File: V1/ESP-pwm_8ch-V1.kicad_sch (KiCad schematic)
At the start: 45 parts, among them J1 12VDC, J2 CH1/2, J3 CH3/4, J4 CH5/6, J5 CH7/8, Q1 IRLB8721PBF, Q2 IRLB8721PBF, Q3 IRLB8721PBF, Q4 IRLB8721PBF, Q5 IRLB8721PBF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

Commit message: work in progress
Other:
- title: ESP 6x PWM Module -> ESP 8x PWM Module
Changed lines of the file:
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@@
   (paper "A3")
   (title_block
-    (title "ESP 6x PWM Module")
+    (title "ESP 8x PWM Module")
     (date "2022-03-26")
     (rev "2")

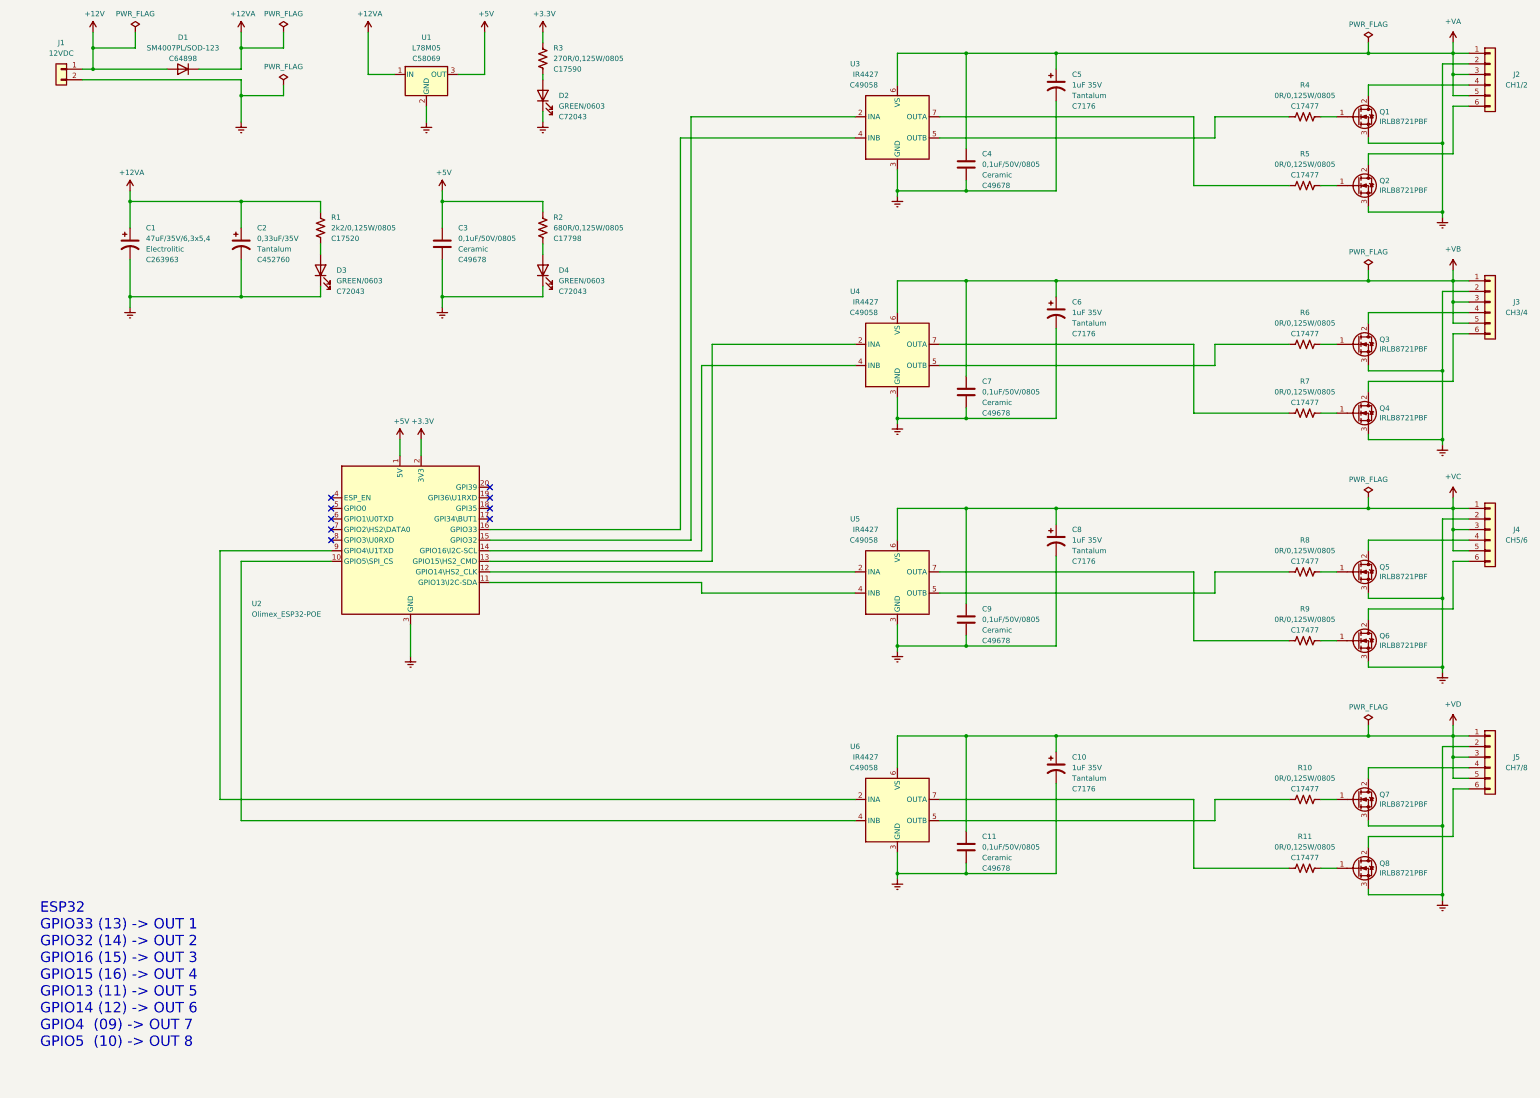
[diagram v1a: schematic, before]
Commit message: Updated MOSFET gate resistor
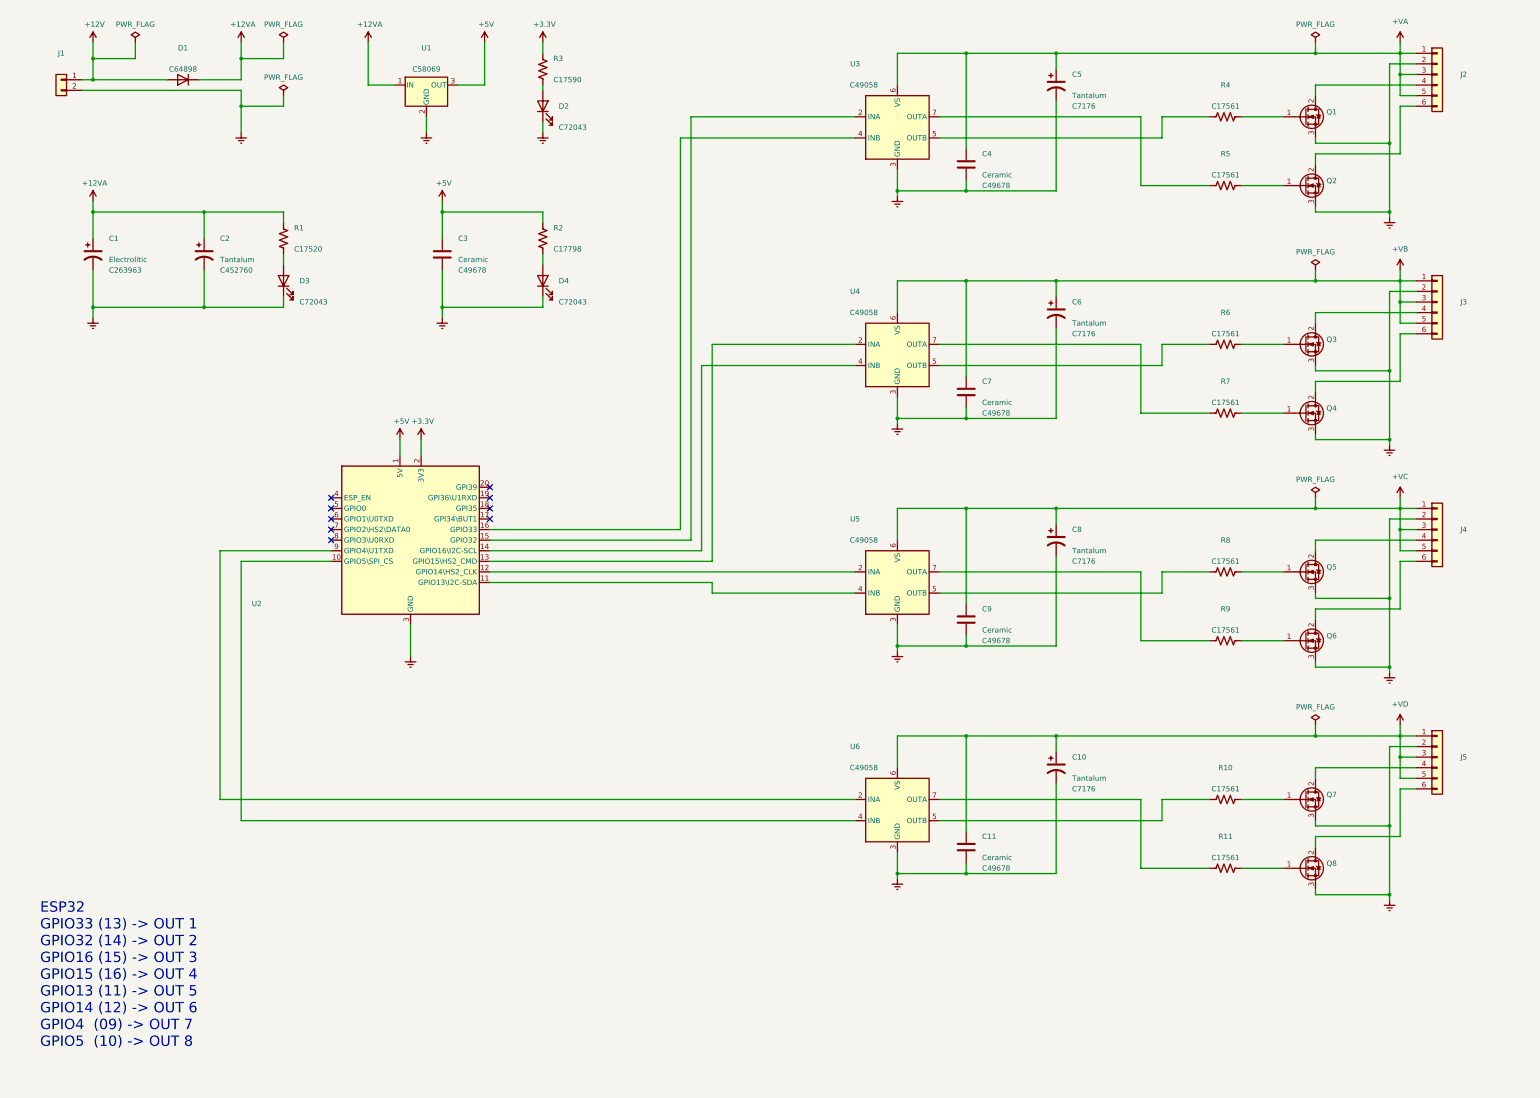
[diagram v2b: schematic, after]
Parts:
- C1: value 47uF/35V/6,3x5,4 -> (none); footprint Tales:CP_Elec_6.3x5.4 -> (none)
- C10, C5, C6, C8: value 1uF 35V -> (none); footprint Tales:CP_EIA-3216-18_Kemet-A_Pad1.58x1.35mm_HandSolder -> (none)
- C11, C3, C4, C7, C9: value 0,1uF/50V/0805 -> (none); footprint Tales:C_0805_2012Metric -> (none)
- C2: value 0,33uF/35V -> (none); footprint Tales:CP_EIA-3216-18_Kemet-A_Pad1.58x1.35mm_HandSolder -> (none)
- D1: value SM4007PL/SOD-123 -> (none); footprint Tales:D_SOD-123 -> (none)
- D2, D3, D4: value GREEN/0603 -> (none); footprint Tales:LED_0603_1608Metric -> (none)
- J1: value 12VDC -> (none); footprint Tales:TerminalBlock_Phoenix_MKDS-3-2-5.08_1x02_P5.08mm_Horizontal -> (none)
- J2: value CH1/2 -> (none); footprint Tales:TerminalBlock_Phoenix_MKDS-3-6-5.08_1x06_P5.08mm_Horizontal -> (none)
- J3: value CH3/4 -> (none); footprint Tales:TerminalBlock_Phoenix_MKDS-3-6-5.08_1x06_P5.08mm_Horizontal -> (none)
- J4: value CH5/6 -> (none); footprint Tales:TerminalBlock_Phoenix_MKDS-3-6-5.08_1x06_P5.08mm_Horizontal -> (none)
- J5: value CH7/8 -> (none); footprint Tales:TerminalBlock_Phoenix_MKDS-3-6-5.08_1x06_P5.08mm_Horizontal -> (none)
- Q1, Q2, Q3, Q4, Q5, Q6, Q7, Q8: value IRLB8721PBF -> (none); footprint Tales:TO-220-3_Vertical -> (none)
- R1: value 2k2/0,125W/0805 -> (none); footprint Tales:R_0805_2012Metric -> (none)
- R10, R11, R4, R5, R6, R7, R8, R9: value 0R/0,125W/0805 -> (none); footprint Tales:R_0805_2012Metric -> (none); LCSC Part C17477 -> C17561; Mfr PN 0805W8F0000T5E -> 0805W8F220JT5E; Vendor PN C17477 -> C17561
- R2: value 680R/0,125W/0805 -> (none); footprint Tales:R_0805_2012Metric -> (none)
- R3: value 270R/0,125W/0805 -> (none); footprint Tales:R_0805_2012Metric -> (none)
- U1: value L78M05 -> (none); footprint Tales:TO-252-2 -> (none)
- U2: value Olimex_ESP32-POE -> (none); footprint Tales:Olimex_ESP32-POE_Pads -> (none)
- U3, U4, U5, U6: value IR4427 -> (none); footprint Tales:SOIC-8_3.9x4.9mm_P1.27mm -> (none)
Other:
- moved on the sheet: C1, C2, C3, D1, D2, D3, D4, J1, J2, J3, J4, J5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

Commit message: Added ESP8266
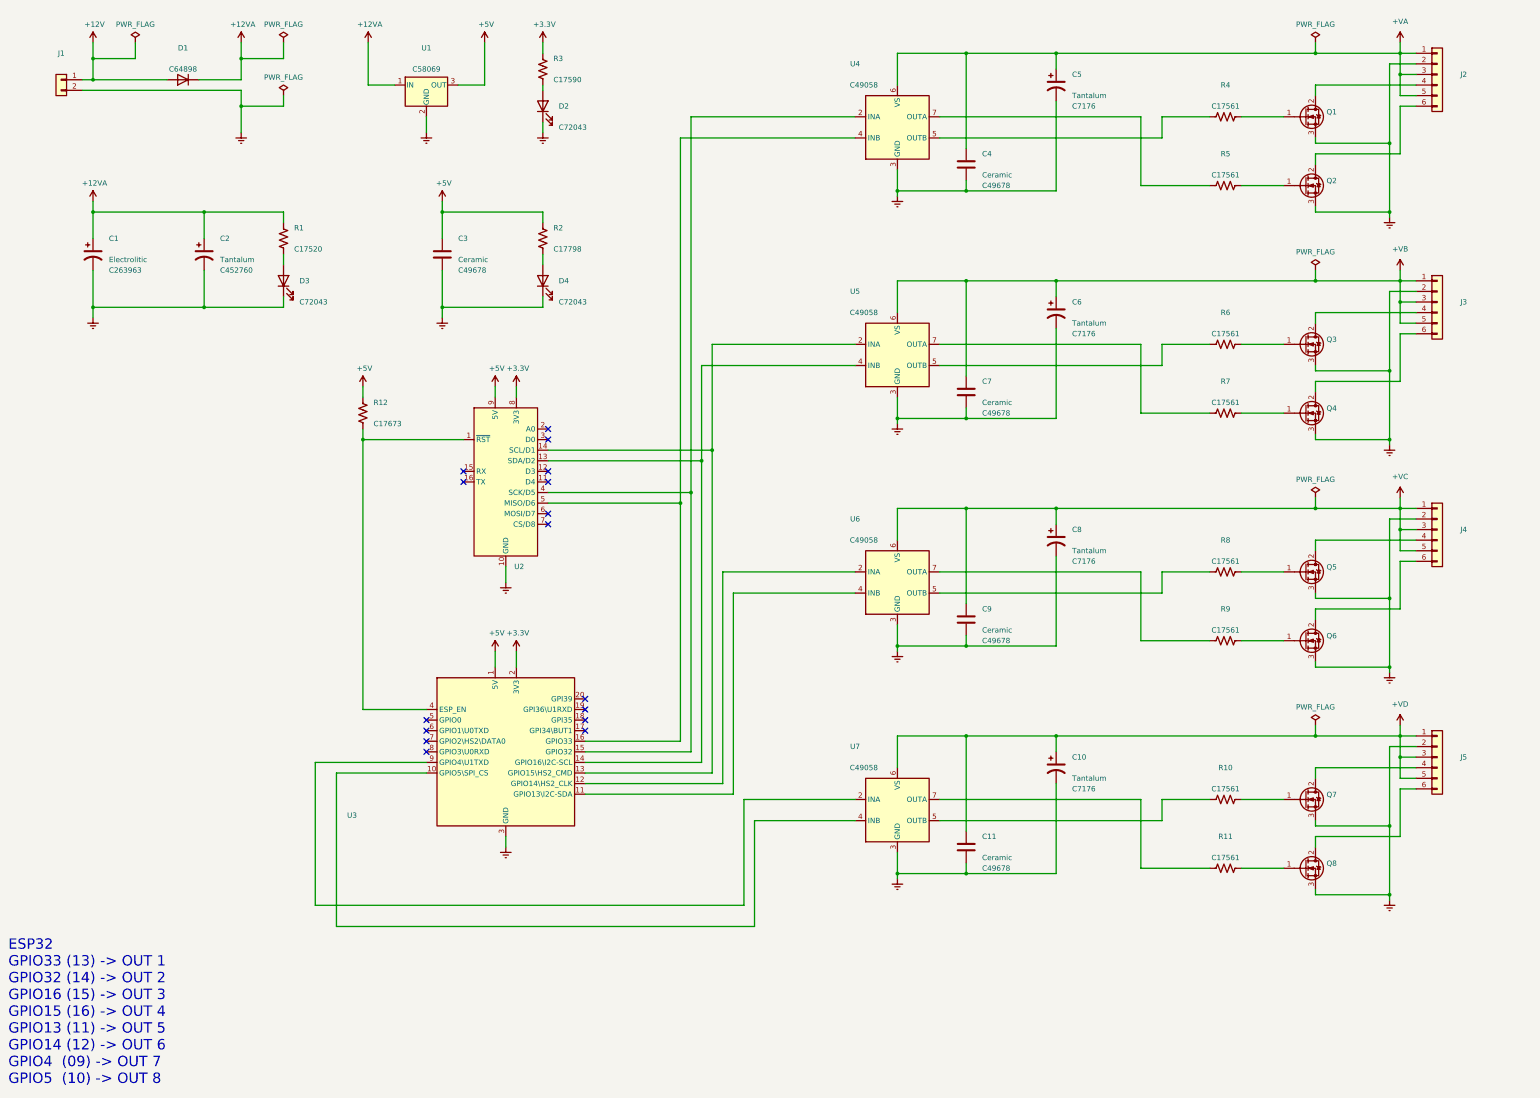
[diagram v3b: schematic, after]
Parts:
- added R12: (no value), symbol Device:R_US
- added U2: (no value), symbol MCU_Module:WeMos_D1_mini
- renumbered U2 to U3, U3 to U4, U4 to U5, U5 to U6, U6 to U7
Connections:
- net +3V3: now also U2.8 (3V3)
- net +5V: now also R12.1, U2.9 (5V)
- net GNDREF: now also U2.10 (GND)
- net at U3.13 (GPIO15\HS2_CMD), U5.2 (INA): now also U2.14 (SCL/D1)
- net at U3.14 (GPIO16\I2C-SCL), U5.4 (INB): now also U2.13 (SDA/D2)
- net at U3.15 (GPIO32), U4.2 (INA): now also U2.4 (SCK/D5)
- net at U3.16 (GPIO33), U4.4 (INB): now also U2.5 (MISO/D6)
- net at U3.4 (ESP_EN): now also R12.2, U2.1 (~{RST})
- no-connect marks 9 -> 16
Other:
- moved on the sheet: U3

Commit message: Reset pull up to +3.3V
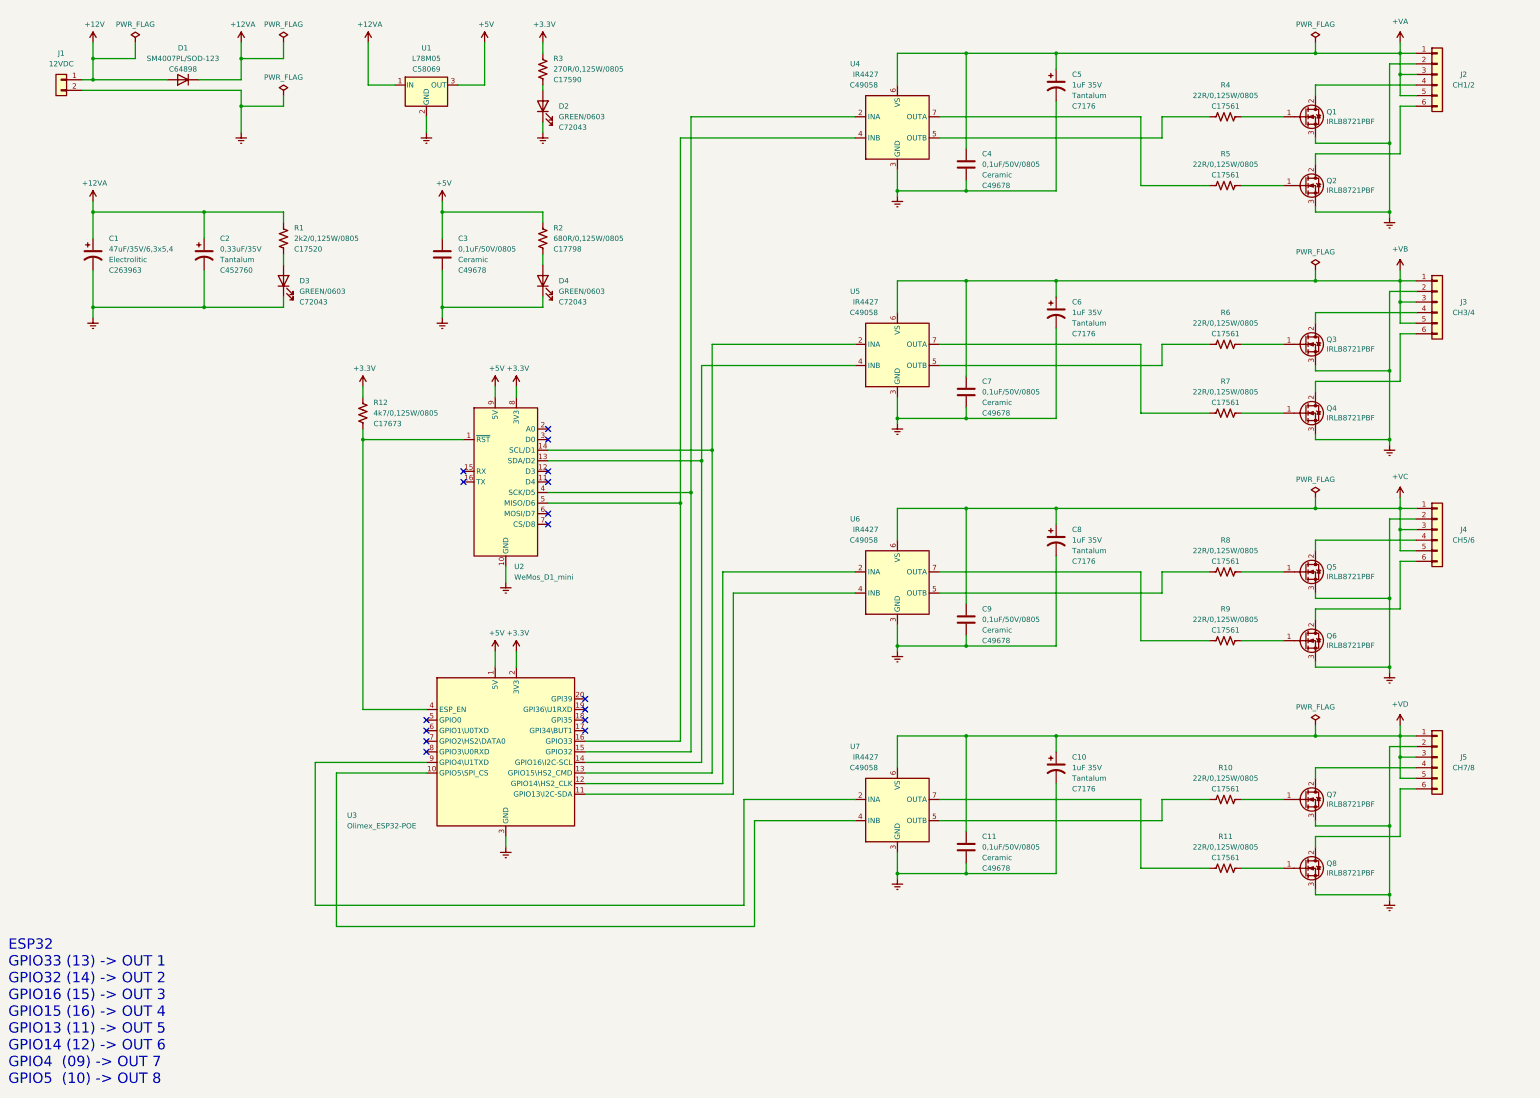
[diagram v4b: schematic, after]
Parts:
- C1: value (none) -> 47uF/35V/6,3x5,4; footprint (none) -> Tales:CP_Elec_6.3x5.4
- C10, C5, C6, C8: value (none) -> 1uF 35V; footprint (none) -> Tales:CP_EIA-3216-18_Kemet-A_Pad1.58x1.35mm_HandSolder
- C11, C3, C4, C7, C9: value (none) -> 0,1uF/50V/0805; footprint (none) -> Tales:C_0805_2012Metric
- C2: value (none) -> 0,33uF/35V; footprint (none) -> Tales:CP_EIA-3216-18_Kemet-A_Pad1.58x1.35mm_HandSolder
- D1: value (none) -> SM4007PL/SOD-123; footprint (none) -> Tales:D_SOD-123
- D2, D3, D4: value (none) -> GREEN/0603; footprint (none) -> Tales:LED_0603_1608Metric
- J1: value (none) -> 12VDC; footprint (none) -> Tales:TerminalBlock_Phoenix_MKDS-3-2-5.08_1x02_P5.08mm_Horizontal
- J2: value (none) -> CH1/2; footprint (none) -> Tales:TerminalBlock_Phoenix_MKDS-3-6-5.08_1x06_P5.08mm_Horizontal
- J3: value (none) -> CH3/4; footprint (none) -> Tales:TerminalBlock_Phoenix_MKDS-3-6-5.08_1x06_P5.08mm_Horizontal
- J4: value (none) -> CH5/6; footprint (none) -> Tales:TerminalBlock_Phoenix_MKDS-3-6-5.08_1x06_P5.08mm_Horizontal
- J5: value (none) -> CH7/8; footprint (none) -> Tales:TerminalBlock_Phoenix_MKDS-3-6-5.08_1x06_P5.08mm_Horizontal
- Q1, Q2, Q3, Q4, Q5, Q6, Q7, Q8: value (none) -> IRLB8721PBF; footprint (none) -> Tales:TO-220-3_Vertical
- R1: value (none) -> 2k2/0,125W/0805; footprint (none) -> Tales:R_0805_2012Metric
- R10, R11, R4, R5, R6, R7, R8, R9: value (none) -> 22R/0,125W/0805; footprint (none) -> Tales:R_0805_2012Metric
- R12: value (none) -> 4k7/0,125W/0805; footprint (none) -> Tales:R_0805_2012Metric
- R2: value (none) -> 680R/0,125W/0805; footprint (none) -> Tales:R_0805_2012Metric
- R3: value (none) -> 270R/0,125W/0805; footprint (none) -> Tales:R_0805_2012Metric
- U1: value (none) -> L78M05; footprint (none) -> Tales:TO-252-2
- U2: value (none) -> WeMos_D1_mini; footprint (none) -> Tales:WEMOS_D1_mini_light_pads
- U3: value (none) -> Olimex_ESP32-POE; footprint (none) -> Tales:Olimex_ESP32-POE_Pads
- U4, U5, U6, U7: value (none) -> IR4427; footprint (none) -> Tales:SOIC-8_3.9x4.9mm_P1.27mm
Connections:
- net +3V3: now also R12.1
- net +5V: no longer R12.1

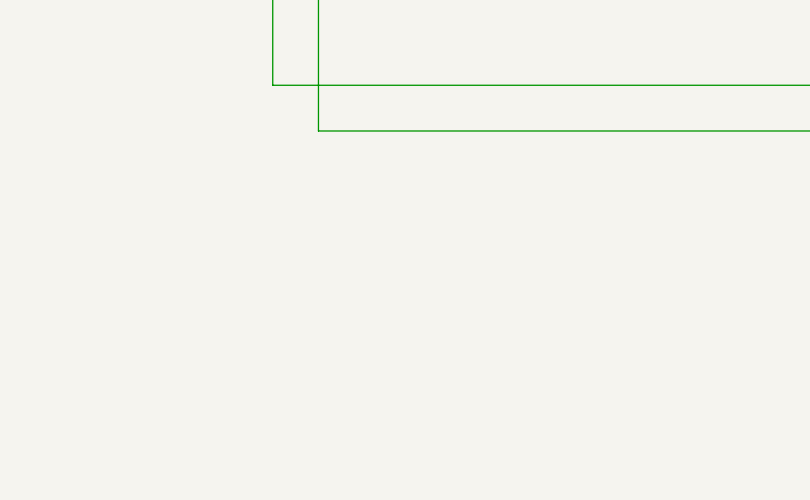
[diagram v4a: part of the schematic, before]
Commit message: Update ESP-pwm_8ch-V1.kicad_sch
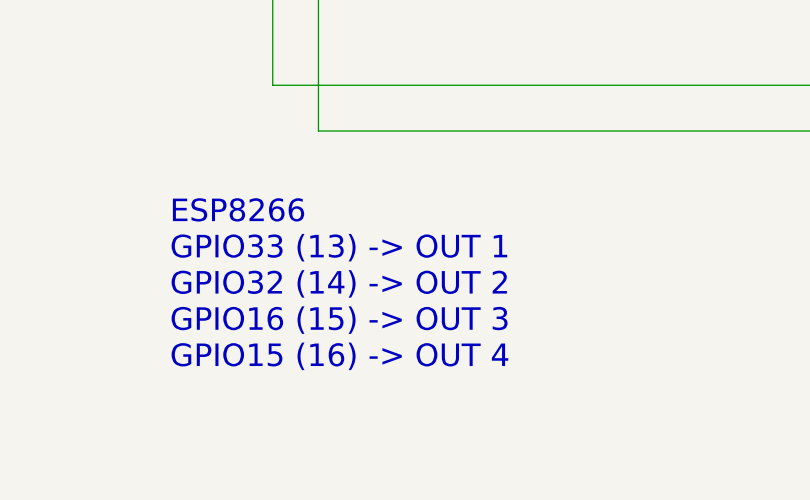
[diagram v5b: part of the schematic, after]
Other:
- note added: "ESP8266 GPIO33 (13) -> OUT 1 GPIO32 (14) -> OUT 2 GPIO16 (15) -> OUT 3 GPIO15 (16) -> OUT 4"
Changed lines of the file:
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@@
     (stroke (width 0) (type default) (color 0 0 0 0))
+  )
+  (text "ESP8266\nGPIO33 (13) -> OUT 1\nGPIO32 (14) -> OUT 2\nGPIO16 (15) -> OUT 3\nGPIO15 (16) -> OUT 4\n"
+    (at 82.55 266.7 0)
+    (effects (font (size 2.5 2.5)) (justify left bottom))
   )
   (text "ESP32\nGPIO33 (13) -> OUT 1\nGPIO32 (14) -> OUT 2\nGPIO16 (15) -> OUT 3\nGPIO15 (16) -> OUT 4\nGPIO13 (11) -> OUT 5\nGPIO14 (12) -> OUT 6\nGPIO4  (09) -> OUT 7\nGPIO5  (10) -> OUT 8"
